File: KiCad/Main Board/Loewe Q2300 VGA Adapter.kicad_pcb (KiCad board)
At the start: 2 copper layers, 65 x 50.8 mm, 63 parts, among them Q1 BC847B, Q10 BC847B, Q14 BC847B, Q2 BC847B, Q3 BC847B, Q4 BC847B, Q5 BC847B, Q6 BC847B, U1 74HCT86

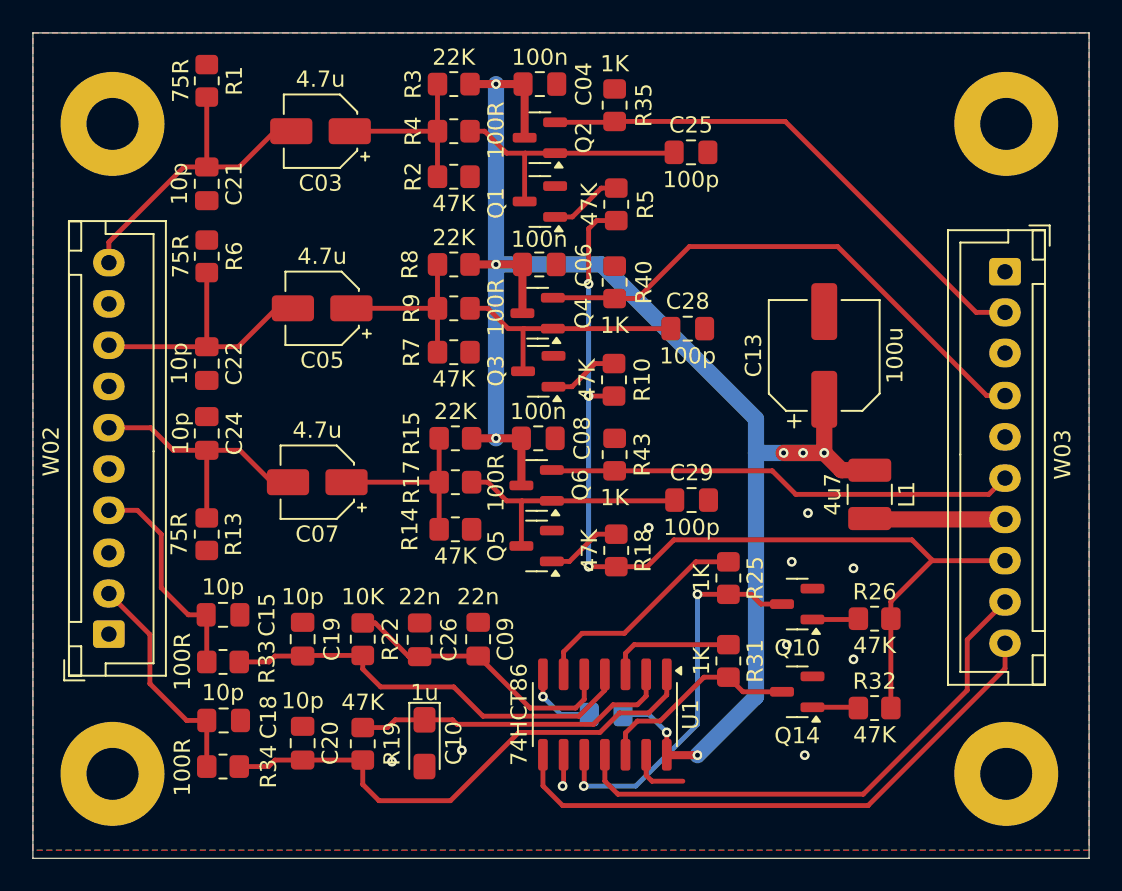
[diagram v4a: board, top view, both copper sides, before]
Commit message: Replace footprint for RGB input capacitors with custom combined SMD/THT one.
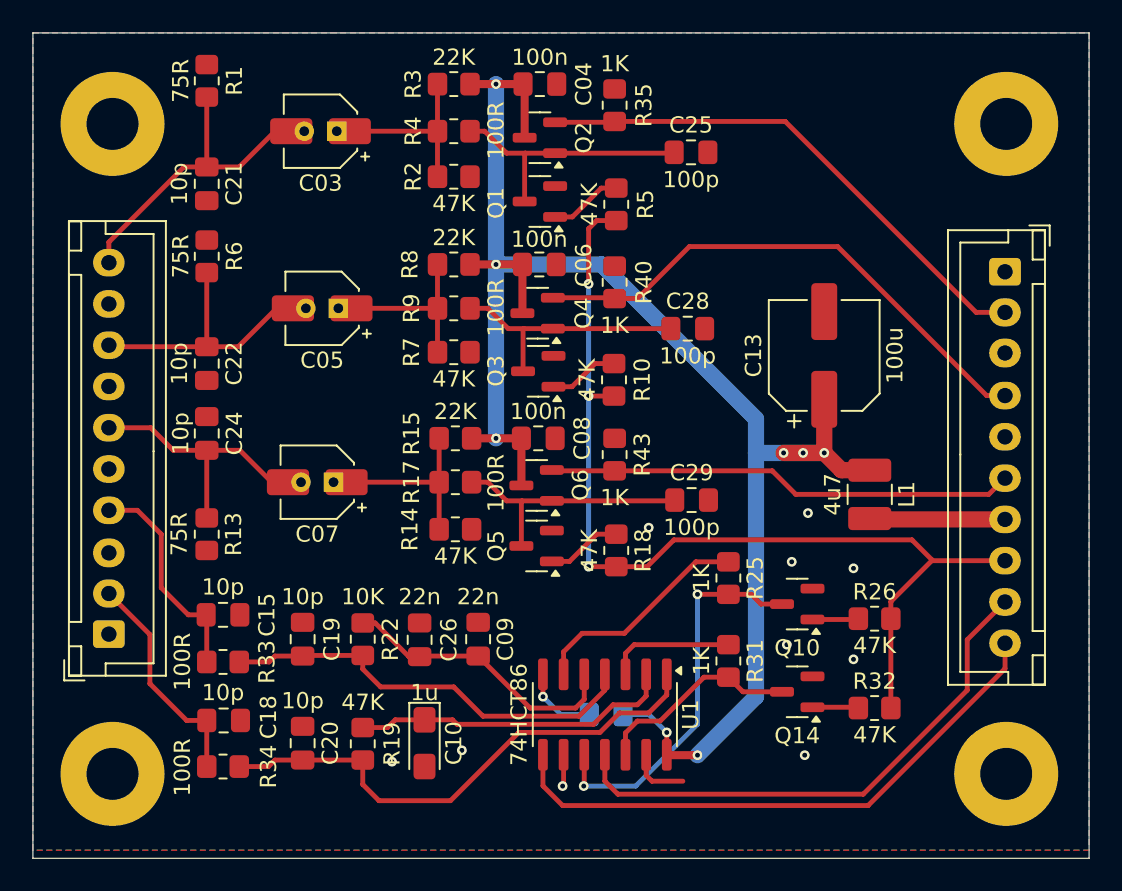
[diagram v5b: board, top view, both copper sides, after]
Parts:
- C03, C05, C07: footprint Capacitor_SMD:CP_Elec_4x5.4 -> Capacitor_SMD_THT:CP_Elec_4x5.4
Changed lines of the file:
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@@
 	(net 32 "Net-(C05-Pad1)")
 	(net 33 "Net-(C07-Pad1)")
-	(footprint "Capacitor_SMD:CP_Elec_4x5.4"
+	(footprint "Capacitor_SMD_THT:CP_Elec_4x5.4"
 		(layer "F.Cu")
 		(at 60.7 72.45 180)
@@
 		(property "Value" "4.7u"
 			(at 0 3.2 180)
-			(layer "F.SilkS")
+			(layer "F.Fab")
 			(effects
 				(font
@@
 			)
 		)
-		(property "Footprint" "Capacitor_SMD:CP_Elec_4x5.4"
+		(property "Footprint" "Capacitor_SMD_THT:CP_Elec_4x5.4"
 			(at 0 0 180)
 			(unlocked yes)
@@
 		(sheetname "Root")
 		(sheetfile "Loewe Q2300 VGA Adapter.kicad_sch")
-		(attr smd)
+		(attr through_hole)
 		(fp_line
 			(start 2.26 2.26)
@@
 			(pintype "passive")
 		)
+		(pad "1" thru_hole rect
+			(at -1 0 180)
+			(size 1.2 1.2)
+			(drill 0.6)
+			(layers "*.Cu" "*.Mask")
+			(remove_unused_layers no)
+			(net 33 "Net-(C07-Pad1)")
+			(pintype "passive")
+		)
+		(pad "2" thru_hole circle
+			(at 1 0 180)
+			(size 1.2 1.2)
+			(drill 0.6)
+			(layers "*.Cu" "*.Mask")
+			(remove_unused_layers no)
+			(net 5 "/BLUE")
+			(pintype "passive")
+		)
 		(pad "2" smd roundrect
 			(at 1.8 0 180)
@@
 			(at 11.25 -3.55 90)
 			(layer "F.SilkS")
+			(hide yes)
 			(effects
 				(font
@@
 		(tags "connector JST XH side entry")
 		(property "Reference" "W03"
-			(at 11.25 -3.55 -90)
+			(at 11.25 -3.55 270)
 			(layer "F.SilkS")
+			(hide yes)
 			(effects
 				(font
@@
 		)
 	)
-	(footprint "Capacitor_SMD:CP_Elec_4x5.4"
+	(footprint "Capacitor_SMD_THT:CP_Elec_4x5.4"
 		(layer "F.Cu")
 		(at 61 61.75 180)
@@
 		(property "Value" "4.7u"
 			(at 0 3.2 180)
-			(layer "F.SilkS")
+			(layer "F.Fab")
 			(effects
 				(font
@@
 			)
 		)
-		(property "Footprint" "Capacitor_SMD:CP_Elec_4x5.4"
+		(property "Footprint" "Capacitor_SMD_THT:CP_Elec_4x5.4"
 			(at 0 0 180)
 			(unlocked yes)
@@
 		(sheetname "Root")
 		(sheetfile "Loewe Q2300 VGA Adapter.kicad_sch")
-		(attr smd)
+		(attr through_hole)
 		(fp_line
 			(start 2.26 2.26)
@@
 			(pintype "passive")
 		)
+		(pad "1" thru_hole rect
+			(at -1 0 180)
+			(size 1.2 1.2)
+			(drill 0.6)
+			(layers "*.Cu" "*.Mask")
+			(remove_unused_layers no)
+			(net 32 "Net-(C05-Pad1)")
+			(pintype "passive")
+		)
+		(pad "2" thru_hole circle
+			(at 1 0 180)
+			(size 1.2 1.2)
+			(drill 0.6)
+			(layers "*.Cu" "*.Mask")
+			(remove_unused_layers no)
+			(net 4 "/GREEN")
+			(pintype "passive")
+		)
 		(pad "2" smd roundrect
 			(at 1.8 0 180)
@@
 		)
 	)
-	(footprint "Capacitor_SMD:CP_Elec_4x5.4"
+	(footprint "Capacitor_SMD_THT:CP_Elec_4x5.4"
 		(layer "F.Cu")
 		(at 60.9 50.85 180)
@@
 		(property "Value" "4.7u"
 			(at 0 3.2 180)
-			(layer "F.SilkS")
+			(layer "F.Fab")
 			(effects
 				(font
@@
 			)
 		)
-		(property "Footprint" "Capacitor_SMD:CP_Elec_4x5.4"
+		(property "Footprint" "Capacitor_SMD_THT:CP_Elec_4x5.4"
 			(at 0 0 180)
 			(unlocked yes)
@@
 		(sheetname "Root")
 		(sheetfile "Loewe Q2300 VGA Adapter.kicad_sch")
-		(attr smd)
+		(attr through_hole)
 		(fp_line
 			(start 2.26 2.26)
@@
 			(pintype "passive")
 		)
+		(pad "1" thru_hole rect
+			(at -1 0 180)
+			(size 1.2 1.2)
+			(drill 0.6)
+			(layers "*.Cu" "*.Mask")
+			(remove_unused_layers no)
+			(net 31 "Net-(C03-Pad1)")
+			(pintype "passive")
+		)
+		(pad "2" thru_hole circle
+			(at 1 0 180)
+			(size 1.2 1.2)
+			(drill 0.6)
+			(layers "*.Cu" "*.Mask")
+			(remove_unused_layers no)
+			(net 1 "/RED")
+			(pintype "passive")
+		)
